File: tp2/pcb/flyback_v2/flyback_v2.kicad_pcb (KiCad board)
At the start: 2 copper layers, 100 x 100 mm, 59 parts, among them J1 Connector_3, J10 Connector_2, J11 Connector_3, J2 Connector_3, J3 Connector_3, J4 Connector_3, J5 Connector_3, J6 Connector_3, J7 Terminal_2, J8 Terminal_2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

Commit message: commit v2 sin disipador
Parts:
- removed the J1 at (177.6, 64.0)
- removed the J2 at (186.2, 64.1)
- removed the J3 at (218.8, 44.1)
- removed the J4 at (218.9, 59.8)
- removed the J5 at (216.0, 93.7)
- removed the J6 at (218.4, 110.0)
- removed REF**: ITBA_Bottom, TCLib:ITBA_Bottom
- removed Rbridge1: 0, TCLib:R_0.125W
- added J1: Connector_2, Connector_AMASS:AMASS_XT30U-F_1x02_P5.0mm_Vertical, F.Cu at (177.6, 74.5)
- added J1: Connector_2, TCLib:PinHeader_1x02_P2.54mm_Vertical, F.Cu at (134.9, 24.9)
- added J10: Connector_2, TCLib:PinHeader_1x02_P2.54mm_Vertical, F.Cu at (167.4, 24.9)
- added J2: Connector_2, TCLib:PinHeader_1x02_P2.54mm_Vertical, F.Cu at (139.6, 24.9)
- added J2: Connector_2, Connector_AMASS:AMASS_XT30U-F_1x02_P5.0mm_Vertical, F.Cu at (186.1, 74.6)
- added J3: Connector_2, Connector_AMASS:AMASS_XT30U-F_1x02_P5.0mm_Vertical, F.Cu at (217.6, 43.9)
- added J3: Connector_2, TCLib:PinHeader_1x02_P2.54mm_Vertical, F.Cu at (144.2, 24.9)
- added J4: Connector_2, TCLib:PinHeader_1x02_P2.54mm_Vertical, F.Cu at (148.8, 24.9)
- added J4: Connector_2, Connector_AMASS:AMASS_XT30U-F_1x02_P5.0mm_Vertical, F.Cu at (217.5, 59.9)
- added J5: Connector_2, TCLib:PinHeader_1x02_P2.54mm_Vertical, F.Cu at (153.5, 24.9)
- added J5: Connector_2, Connector_AMASS:AMASS_XT30U-F_1x02_P5.0mm_Vertical, F.Cu at (217.3, 93.7)
- added J6: Connector_2, Connector_AMASS:AMASS_XT30U-F_1x02_P5.0mm_Vertical, F.Cu at (217.1, 109.7)
- added J6: Connector_2, TCLib:PinHeader_1x02_P2.54mm_Vertical, F.Cu at (158.2, 24.9)
- added J9: Connector_2, TCLib:PinHeader_1x02_P2.54mm_Vertical, F.Cu at (162.8, 24.9)
- C5: footprint TCLib:C_5mm -> TCLib:C_2.5mm
- J11: value Connector_3 -> Connector_2; footprint TCLib:PinHeader_1x03_P2.54mm_Vertical -> TCLib:PinHeader_1x02_P2.54mm_Vertical
- R15: value 1Meg -> 2Meg2
- R3: value 58k-1W -> 56k-1W
- moved J11 89.8 mm to (172.1, 24.9), turned to 0 degrees
- moved D4 21.0 mm to (232.3, 64.7), turned to 0 degrees
- moved Q3 17.8 mm to (199.1, 91.5)
- moved R3 13.6 mm to (192.4, 81.4)
- moved C6 13.2 mm to (180.1, 91.9)
- moved D6 12.3 mm to (199.4, 75.1)
- moved C16 9.58 mm to (150.6, 77.1)
- moved J10 9.55 mm to (169.9, 92.1)
- moved C9 9.37 mm to (180.1, 83.1)
- moved C3 8.85 mm to (206.1, 89.7), turned to -90 degrees
- moved R15 8.75 mm to (154.2, 78.0)
- moved R5 7.86 mm to (189.3, 98.5)
- moved C5 7.62 mm to (160.9, 109.8), turned to 0 degrees
- moved J9 7.32 mm to (203.4, 99.3)
- moved J7 7.18 mm to (148.5, 102.3)
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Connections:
- C5 pad 1: Vcol -> Net-(Q1-C)
- J11 pad 1: 16V -> Vin
- J11 pad 2: Vcol -> Vin
- Q1 pad 3: Vcol -> Net-(Q1-C)
- R4 pad 1: Vcol -> Net-(Q1-C)
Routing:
- net GNDREF: track 123.2 -> 26.0 mm
- net GND: track 397.0 -> 318.3 mm
- net Net-(Q3-G): track 35.4 -> 7.96 mm
- net Vrealim: track 116.2 -> 95.8 mm
- net Vcol: track 19.4 -> 0.00 mm
- net Vref: track 49.4 -> 32.8 mm
- net Vin: track 40.1 -> 31.2 mm
- net Net-(C3-Pad1): track 32.6 -> 24.4 mm
- net Net-(D5-PadA): track 24.4 -> 18.1 mm
- net 16V: track 17.1 -> 23.2 mm
- net Net-(Q1-E): track 23.3 -> 28.5 mm
- net Vout: track 29.9 -> 25.7 mm
- net Net-(C4-Pad1): track 16.9 -> 19.9 mm
- net Vlinea: track 10.7 -> 8.70 mm
- net Vneutro: track 17.8 -> 16.0 mm
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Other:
- board text removed: "Convertidor Volar-Atrás"

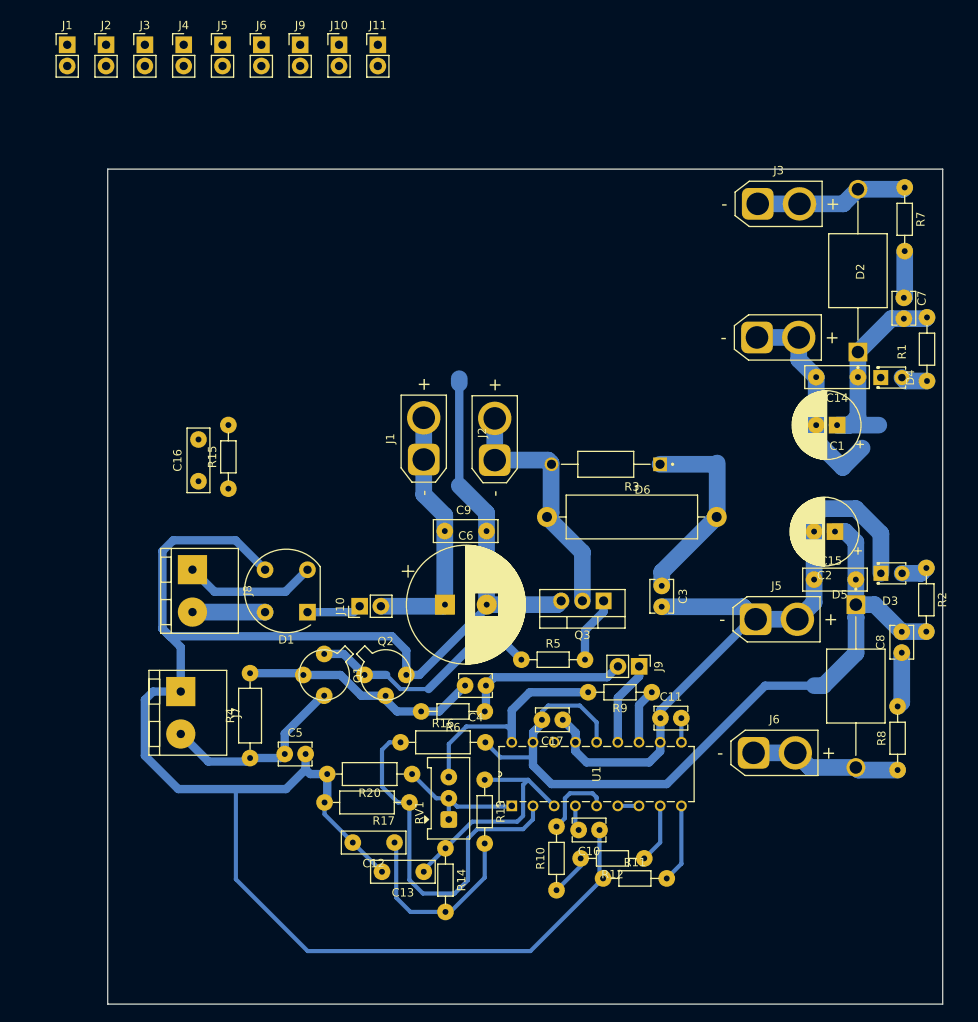
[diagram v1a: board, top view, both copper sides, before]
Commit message: puse el jumper de Vrealim y 16V
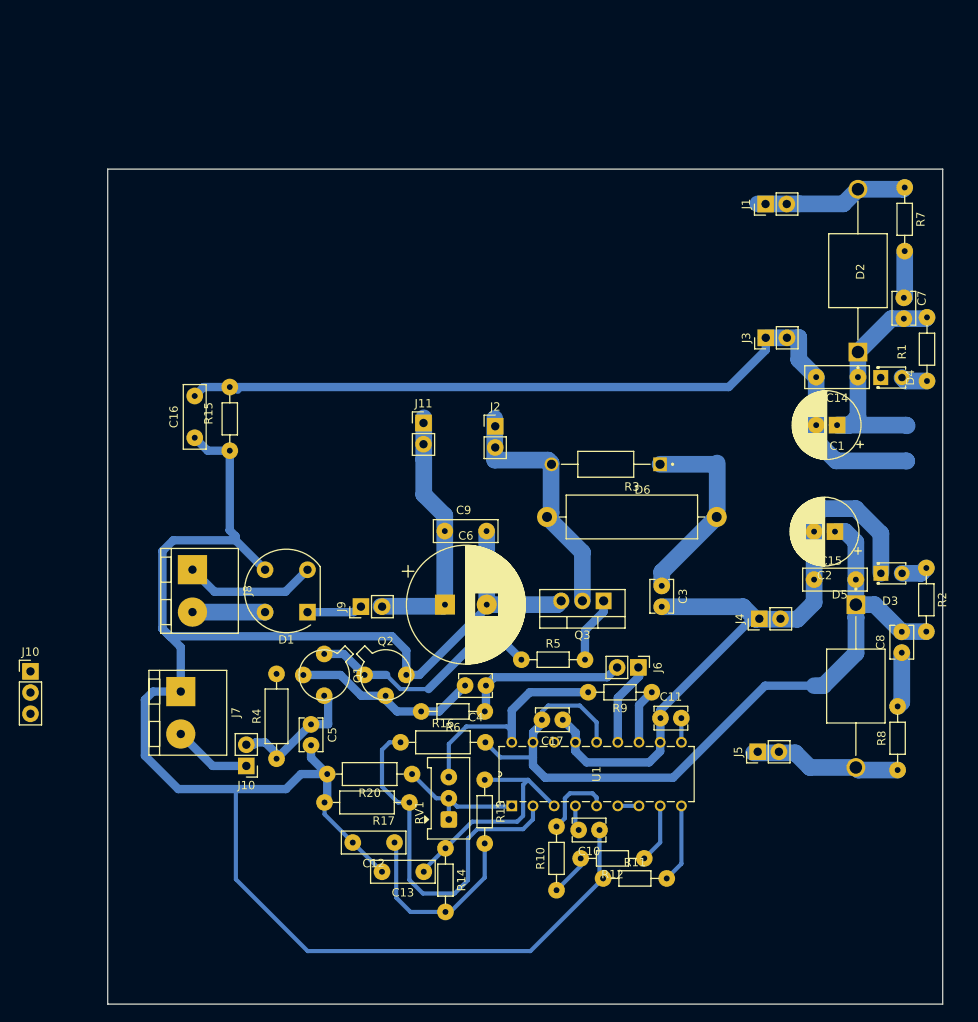
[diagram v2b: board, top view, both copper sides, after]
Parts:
- removed the J1 at (177.6, 74.5)
- removed the J2 at (186.1, 74.6)
- removed the J3 at (217.6, 43.9)
- removed the J4 at (217.5, 59.9)
- removed the J5 at (217.3, 93.7)
- removed the J6 at (217.1, 109.7)
- removed the J9 at (203.4, 99.3)
- J10: value Connector_2 -> Connector_3; footprint TCLib:PinHeader_1x02_P2.54mm_Vertical -> TCLib:PinHeader_1x03_P2.54mm_Vertical
- moved J5 106.2 mm to (217.6, 109.5), turned to 90 degrees
- moved J4 97.4 mm to (217.8, 93.6), turned to 90 degrees
- moved J6 87.2 mm to (203.3, 99.4), turned to -90 degrees
- moved J10 87.1 mm to (156.3, 111.2), turned to 180 degrees
- moved J1 85.8 mm to (218.5, 43.9), turned to 90 degrees
- moved J3 82.2 mm to (218.6, 60.0), turned to 90 degrees
- moved J9 67.7 mm to (170.1, 92.2), turned to 90 degrees
- moved J2 65.3 mm to (186.2, 70.5)
- moved J11 45.6 mm to (177.6, 70.2)
- moved J10 40.2 mm to (130.5, 99.9), turned to 0 degrees
- moved C16 5.23 mm to (150.2, 71.9)
- moved C5 4.75 mm to (164.1, 106.2), turned to -90 degrees
- moved R15 4.55 mm to (154.4, 73.5)
- moved R4 3.17 mm to (160.0, 110.4)
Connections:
- C5 pad 1: Net-(Q1-C) -> Vcol
- J10 pad 1: Net-(D1-+) -> 16V
- J10 pad 2: Vin -> Vcol
- Q1 pad 3: Net-(Q1-C) -> Vcol
- R4 pad 1: Net-(Q1-C) -> Vcol
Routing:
- net GNDREF: track 26.0 -> 102.3 mm
- net Net-(Q1-C): track 0.00 -> 16.6 mm
- net 16V: track 23.2 -> 9.43 mm
- net Net-(Q1-B): track 29.2 -> 23.1 mm
- net Vout: track 25.7 -> 29.1 mm
- net GND: track 318.3 -> 316.4 mm
- net Vrealim: track 95.8 -> 95.2 mm

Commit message: rute finished, + pnies trafo + pdf
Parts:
- removed the J10 at (156.3, 111.2)
- added J10: Connector_3, TCLib:PinHeader_1x03_P2.54mm_Vertical, B.Cu at (161.8, 70.5)
- added J10: Connector_3, TCLib:PinHeader_1x03_P2.54mm_Vertical, B.Cu at (164.3, 70.5)
- added J10: Connector_3, TCLib:PinHeader_1x03_P2.54mm_Vertical, B.Cu at (154.1, 70.5)
- added J10: Connector_3, TCLib:PinHeader_1x03_P2.54mm_Vertical, B.Cu at (156.6, 70.5)
- added J10: Connector_3, TCLib:PinHeader_1x03_P2.54mm_Vertical, B.Cu at (169.4, 70.5)
- added J10: Connector_3, TCLib:PinHeader_1x03_P2.54mm_Vertical, B.Cu at (164.3, 42.8)
- added J10: Connector_3, TCLib:PinHeader_1x03_P2.54mm_Vertical, B.Cu at (171.9, 42.8)
- added J10: Connector_3, TCLib:PinHeader_1x03_P2.54mm_Vertical, B.Cu at (166.9, 42.8)
- added J10: Connector_3, TCLib:PinHeader_1x03_P2.54mm_Vertical, B.Cu at (159.2, 70.5)
- added J10: Connector_3, TCLib:PinHeader_1x03_P2.54mm_Vertical, B.Cu at (174.4, 42.8)
- added J10: Connector_3, TCLib:PinHeader_1x03_P2.54mm_Vertical, B.Cu at (169.4, 42.8)
- added J10: Connector_3, TCLib:PinHeader_1x03_P2.54mm_Vertical, B.Cu at (174.4, 70.5)
- added J10: Connector_3, TCLib:PinHeader_1x03_P2.54mm_Vertical, B.Cu at (159.2, 42.8)
- added J10: Connector_3, TCLib:PinHeader_1x03_P2.54mm_Vertical, B.Cu at (154.1, 42.8)
- added J10: Connector_3, TCLib:PinHeader_1x03_P2.54mm_Vertical, B.Cu at (161.8, 42.8)
- added J10: Connector_3, TCLib:PinHeader_1x03_P2.54mm_Vertical, B.Cu at (156.7, 42.8)
- added J10: Connector_3, TCLib:PinHeader_1x03_P2.54mm_Vertical, B.Cu at (166.9, 70.5)
- added J10: Connector_3, TCLib:PinHeader_1x03_P2.54mm_Vertical, B.Cu at (171.9, 70.5)
- added REF**: ITBA_Bottom, TCLib:ITBA_Bottom, F.Cu at (226.7, 126.0)
- C5: footprint TCLib:C_2.5mm -> TCLib:C_5mm
- J10: moved to B.Cu
- moved J10 29.3 mm to (159.6, 103.2), turned to 180 degrees
- moved D4 20.8 mm to (237.9, 44.7), turned to -90 degrees
- moved C16 8.74 mm to (150.1, 80.7)
- moved R15 8.74 mm to (154.3, 82.2)
- moved J11 5.88 mm to (177.8, 76.0)
- moved R4 3.96 mm to (156.0, 110.3)
- moved J2 3.22 mm to (189.4, 70.6)
- moved C5 1.23 mm to (163.4, 105.3)
- moved R1 0.10 mm to (237.9, 57.4), turned to 90 degrees
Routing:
- net GNDREF: track 102.3 -> 146.6 mm
- net Net-(Q1-C): track 16.6 -> 0.00 mm
- net Vcol: track 0.00 -> 15.2 mm
- net GND: track 316.4 -> 307.4 mm
- net Vin: track 31.2 -> 24.5 mm
- net Net-(Q1-B): track 23.1 -> 29.6 mm
- net 16V: track 9.43 -> 14.5 mm
- net Vdrain: track 30.5 -> 26.0 mm
- net Vrealim': track 44.0 -> 41.6 mm
- net Net-(D4-A): track 3.17 -> 2.56 mm
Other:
- board text added: "Convertidor Flyback Juli - Kramer - Pensa"

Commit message: agregue /output en /pcb
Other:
- board text added: "Convertidor Volar-Atrás V2 Juli - Kramer - Pensa"
- board text removed: "Convertidor Flyback Juli - Kramer - Pensa"
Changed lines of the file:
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@@
 		(tenting front back)
 		(pcbplotparams
-			(layerselection 0x00000000_00000000_55555555_55555570)
+			(layerselection 0x00000000_00000000_55555555_55555554)
 			(plot_on_all_layers_selection 0x00000000_00000000_00000000_02000000)
 			(disableapertmacros no)
@@
 			(subtractmaskfromsilk no)
 			(outputformat 4)
-			(mirror yes)
-			(drillshape 0)
+			(mirror no)
+			(drillshape 2)
 			(scaleselection 1)
-			(outputdirectory "")
+			(outputdirectory "output/")
 		)
 	)
@@
 		(layer "Edge.Cuts")
 	)
-	(gr_text "Convertidor Flyback\nJuli - Kramer - Pensa"
+	(gr_text "Convertidor Volar-Atrás V2\nJuli - Kramer - Pensa"
 		(at 237.29 133.79 0)
 		(layer "B.Cu")
